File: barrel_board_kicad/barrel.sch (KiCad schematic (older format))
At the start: 29 parts, among them J1 220V, J2 12V, J3 probe/prog, J4 valve, J5 Bypass, J6 reset, K1 DIPxx-1Cxx-51x, Q1 Q_PMOS_GSD, Q2 Q_NMOS_GSD, Q3 Q_PMOS_GSD, U1 LM2576S-5, U2 ATtiny13A-SSU

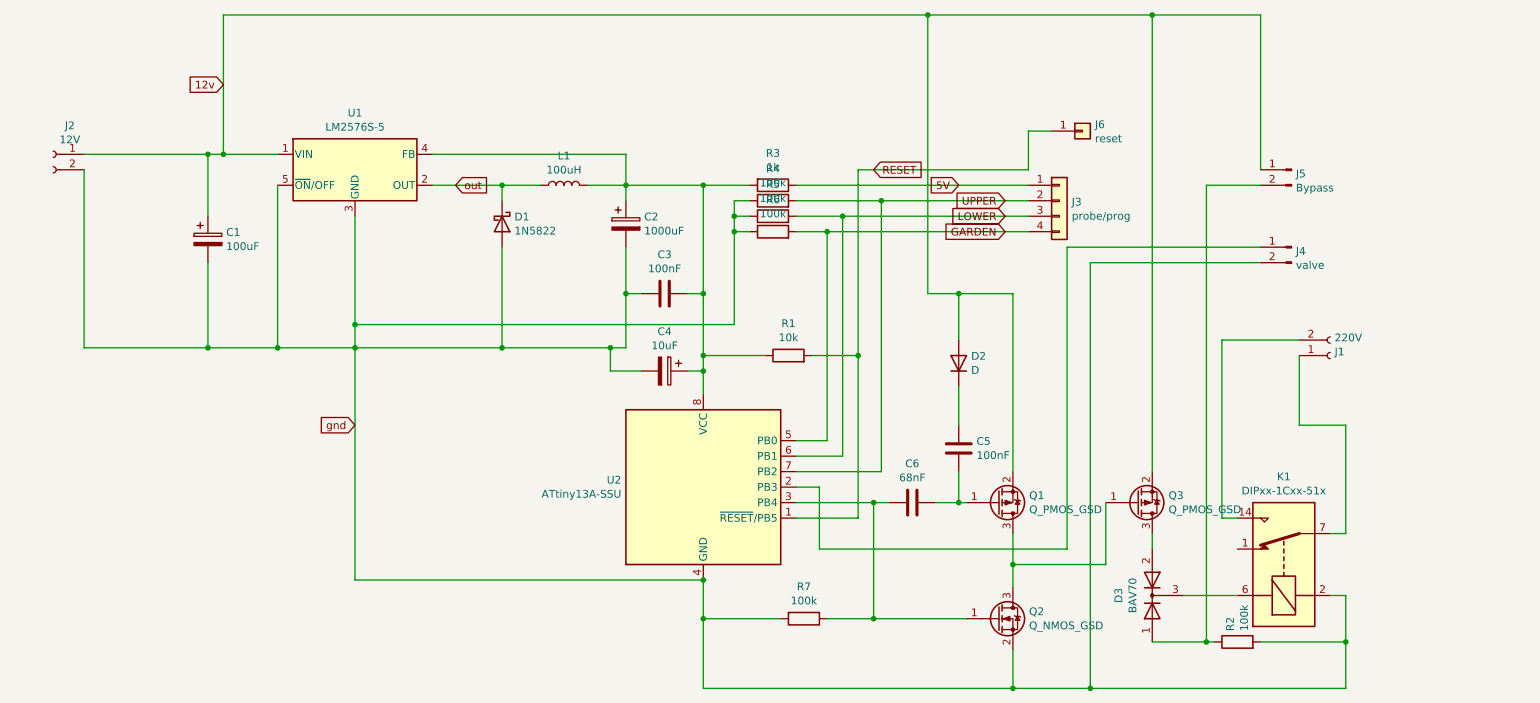
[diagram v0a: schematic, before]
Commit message: Optimize the scheme
Remove redundant transistors
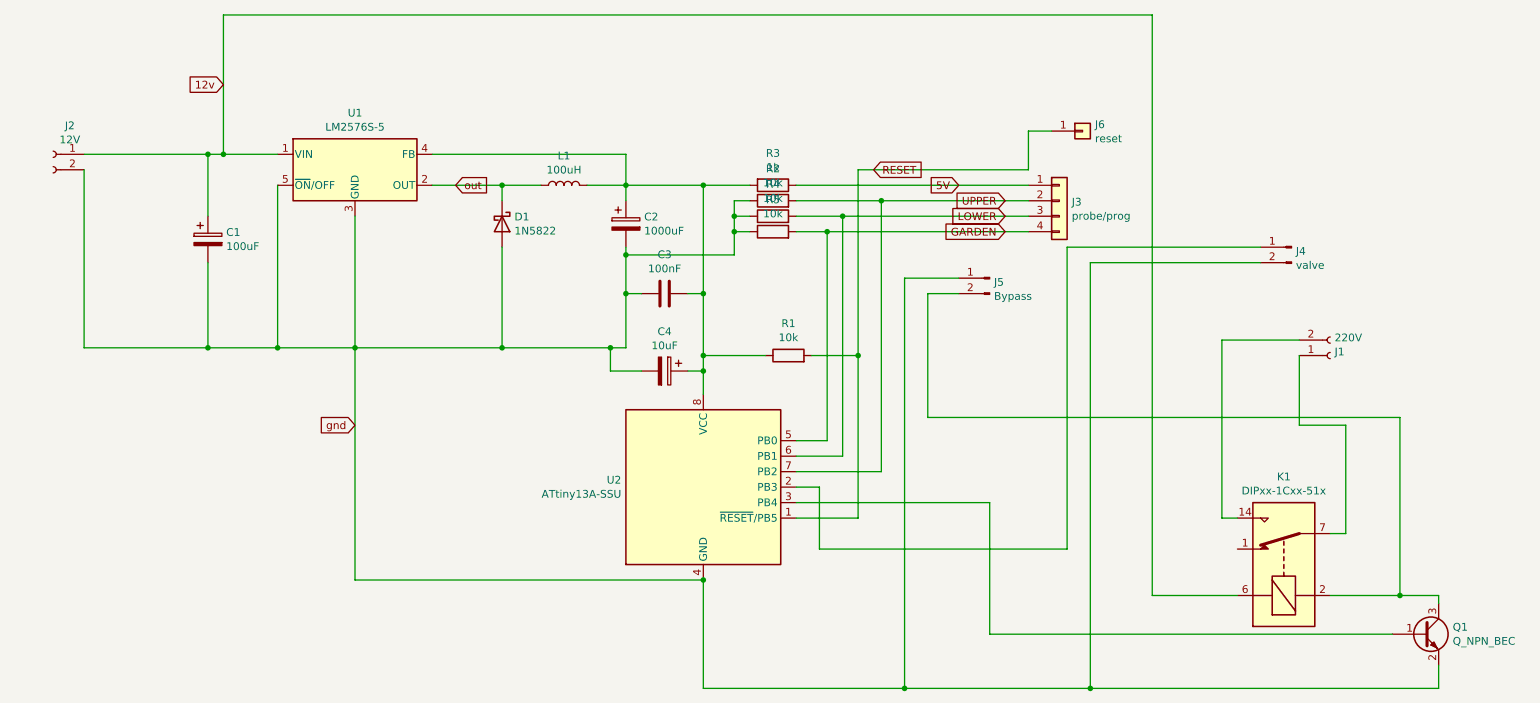
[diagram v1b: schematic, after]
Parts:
- removed C5: 100nF, Capacitor_SMD:C_0805_2012Metric_Pad1.18x1.45mm_HandSolder, symbol Device:C
- removed C6: 68nF, Capacitor_SMD:C_0805_2012Metric_Pad1.18x1.45mm_HandSolder, symbol Device:C
- removed D2: D, Diode_THT:D_A-405_P2.54mm_Vertical_AnodeUp, symbol Device:D
- removed D3: BAV70, Package_TO_SOT_SMD:SOT-23, symbol Diode:BAV70
- removed Q1, Q3: Q_PMOS_GSD, Package_TO_SOT_SMD:SOT-23, symbol Device:Q_PMOS_GSD
- removed Q2: Q_NMOS_GSD, Package_TO_SOT_SMD:SOT-23, symbol Device:Q_NMOS_GSD
- removed R6, R7: 100k, Resistor_SMD:R_0805_2012Metric_Pad1.20x1.40mm_HandSolder, symbol Device:R
- added Q1: Q_NPN_BEC, Package_TO_SOT_SMD:SOT-23, symbol Device:Q_NPN_BEC
- R2, R4, R5: value 100k -> 10k
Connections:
- net 12v: now also K1.6; no longer J5.1 (Pin_1)
- net GARDEN: now also R5.2
- net LOWER: now also R4.2; no longer R5.2
- net UPPER: now also R2.2; no longer R4.2
- net gnd: now also J5.1 (Pin_1), R2.1, Q1.2 (E); no longer K1.2, R2.2
- net at U2.3 (PB4): now also Q1.1 (B)
- net at J5.2 (Pin_2): now also K1.2, Q1.3 (C); no longer R2.1
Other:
- moved on the sheet: J5

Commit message: Fix relay scheme
Add a resistor for the transistor that controlls relay to be in a defined state at startup
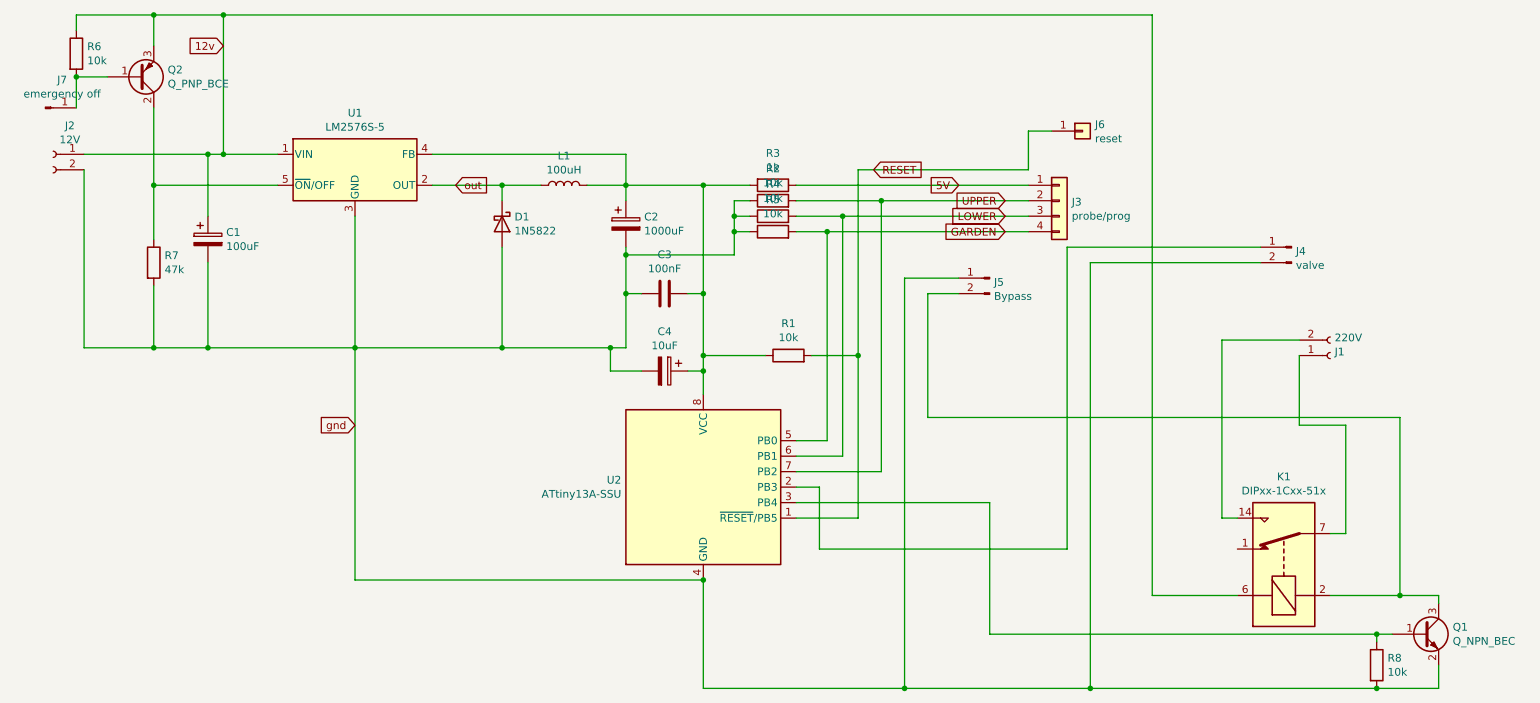
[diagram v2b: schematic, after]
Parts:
- added J7: emergency off, Connector_PinHeader_2.54mm:PinHeader_1x01_P2.54mm_Vertical, symbol Connector:Conn_01x01_Male
- added Q2: Q_PNP_BCE, Package_TO_SOT_SMD:SOT-23, symbol Device:Q_PNP_BCE
- added R6, R8: 10k, Resistor_SMD:R_0805_2012Metric_Pad1.20x1.40mm_HandSolder, symbol Device:R
- added R7: 47k, Resistor_SMD:R_0805_2012Metric_Pad1.20x1.40mm_HandSolder, symbol Device:R
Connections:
- net 12v: now also Q2.3 (E), R6.1
- net gnd: now also R7.2, R8.2; no longer U1.5 (~ON~/OFF)
- net at Q1.1 (B), U2.3 (PB4): now also R8.1
- new net: Q2.2 (C), R7.1, U1.5 (~ON~/OFF)
- new net: J7.1 (Pin_1), Q2.1 (B), R6.2
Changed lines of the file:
@@
 	900  2750 900  3900
 Wire Wire Line
-	900  3900 1700 3900
+	900  3900 1350 3900
 Connection ~ 1700 3900
-Wire Wire Line
-	1700 3900 2150 3900
 Wire Wire Line
 	1800 2650 1800 1750
 Connection ~ 1800 2650
-Wire Wire Line
-	1800 2650 2150 2650
 Connection ~ 1700 2650
 Wire Wire Line
 	1700 2650 1800 2650
-Wire Wire Line
-	2150 2850 2150 3900
-Connection ~ 2150 3900
-Wire Wire Line
-	2150 3900 2650 3900
 Text GLabel 6550 2850 0    50   Input ~ 0
 5V
@@
 Wire Wire Line
 	6050 4700 6050 2950
-Text GLabel 1800 2200 0    50   Input ~ 0
+Text GLabel 1800 1950 0    50   Input ~ 0
 12v
 Text GLabel 2650 4400 0    50   Input ~ 0
@@
 $EndComp
 Wire Wire Line
-	7400 6100 9650 6100
+	7400 6100 9250 6100
 Wire Wire Line
 	9650 5500 9650 5550
@@
 	6750 4900 6750 5750
 Wire Wire Line
-	6750 5750 9350 5750
+	6750 5750 9250 5750
 Wire Wire Line
 	6550 3550 6350 3550
@@
 Wire Wire Line
 	5100 3150 5100 3300
+Wire Wire Line
+	1700 3900 2650 3900
+$Comp
+L Device:Q_PNP_BCE Q2
+U 1 1 61183751
+P 1250 2150
+F 0 "Q2" H 1440 2104 50  0000 L CNN
+F 1 "Q_PNP_BCE" H 1440 2195 50  0000 L CNN
+F 2 "Package_TO_SOT_SMD:SOT-23" H 1450 2250 50  0001 C CNN
+F 3 "~" H 1250 2150 50  0001 C CNN
+	1    1250 2150
+	1    0    0    1
+$EndComp
+Wire Wire Line
+	1800 2650 2150 2650
+Wire Wire Line
+	1800 1750 1350 1750
+Wire Wire Line
+	1350 1750 1350 1950
+Connection ~ 1800 1750
+Wire Wire Line
+	1350 2350 1350 2850
+Wire Wire Line
+	1350 2850 2150 2850
+$Comp
+L Device:R R7
+U 1 1 6118FD3C
+P 1350 3350
+F 0 "R7" H 1420 3396 50  0000 L CNN
+F 1 "47k" H 1420 3305 50  0000 L CNN
+F 2 "Resistor_SMD:R_0805_2012Metric_Pad1.20x1.40mm_HandSolder" V 1280 3350 50  0001 C CNN
+F 3 "~" H 1350 3350 50  0001 C CNN
+	1    1350 3350
+	1    0    0    -1
+$EndComp
+$Comp
+L Device:R R6
+U 1 1 61190DCA
+P 850 2000
+F 0 "R6" H 920 2046 50  0000 L CNN
+F 1 "10k" H 920 1955 50  0000 L CNN
+F 2 "Resistor_SMD:R_0805_2012Metric_Pad1.20x1.40mm_HandSolder" V 780 2000 50  0001 C CNN
+F 3 "~" H 850 2000 50  0001 C CNN
+	1    850  2000
+	1    0    0    -1
+$EndComp
+Wire Wire Line
+	850  2150 1050 2150
+Wire Wire Line
+	1350 1750 850  1750
+Wire Wire Line
+	850  1750 850  1850
+Connection ~ 1350 1750
+$Comp
+L Connector:Conn_01x01_Male J7
+U 1 1 611978EF
+P 650 2350
+F 0 "J7" H 758 2531 50  0000 C CNN
+F 1 "emergency off" H 758 2440 50  0000 C CNN
+F 2 "Connector_PinHeader_2.54mm:PinHeader_1x01_P2.54mm_Vertical" H 650 2350 50  0001 C CNN
+F 3 "~" H 650 2350 50  0001 C CNN
+	1    650  2350
+	1    0    0    -1
+$EndComp
+Wire Wire Line
+	850  2150 850  2350
+Connection ~ 850  2150
+Wire Wire Line
+	1350 2850 1350 3200
+Connection ~ 1350 2850
+Wire Wire Line
+	1350 3500 1350 3900
+Connection ~ 1350 3900
+Wire Wire Line
+	1350 3900 1700 3900
+$Comp
+L Device:R R8
+U 1 1 611AB0D0
+P 9250 5950
+F 0 "R8" H 9320 5996 50  0000 L CNN
+F 1 "10k" H 9320 5905 50  0000 L CNN
+F 2 "Resistor_SMD:R_0805_2012Metric_Pad1.20x1.40mm_HandSolder" V 9180 5950 50  0001 C CNN
+F 3 "~" H 9250 5950 50  0001 C CNN
+	1    9250 5950
+	1    0    0    -1
+$EndComp
+Connection ~ 9250 6100
+Wire Wire Line
+	9250 6100 9650 6100
+Wire Wire Line
+	9250 5800 9250 5750
+Connection ~ 9250 5750
+Wire Wire Line
+	9250 5750 9350 5750
 $EndSCHEMATC
